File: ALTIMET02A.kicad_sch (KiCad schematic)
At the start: 11 parts

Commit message: Edit schema.
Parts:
- removed J? (x2): Conn_01x03_Male, symbol Connector:Conn_01x03_Male
- removed J? (x2): Conn_02x03_Odd_Even, symbol Connector_Generic:Conn_02x03_Odd_Even
- removed J?: Conn_02x06_Odd_Even, symbol Connector_Generic:Conn_02x06_Odd_Even
- added C?: 100nF, Capacitor_SMD:C_0805_2012Metric, symbol Device:C
- added J?: HEADER_2x05_PARALLEL, Mlab_Pin_Headers:Straight_2x05, symbol MLAB_HEADER:HEADER_2x05_PARALLEL
- added J?: HEADER_2x03_PARALLEL, Mlab_Pin_Headers:Straight_2x03, symbol MLAB_HEADER:HEADER_2x03_PARALLEL
- added J?: HEADER_2x03, Mlab_Pin_Headers:Straight_2x03, symbol MLAB_HEADER:HEADER_2x03
- added JP? (x2): SolderJumper_3_Bridged12, Jumper:SolderJumper-3_P1.3mm_Bridged12_RoundedPad1.0x1.5mm_NumberLabels, symbol Jumper:SolderJumper_3_Bridged12
- added JP?: SolderJumper_3_Bridged123, Jumper:SolderJumper-3_P1.3mm_Bridged12_RoundedPad1.0x1.5mm_NumberLabels, symbol Jumper:SolderJumper_3_Bridged123
- C?: value 100nF -> 10uF; footprint (none) -> Capacitor_SMD:C_0805_2012Metric
- H? (x4): footprint (none) -> Mlab_Mechanical:MountingHole_3mm
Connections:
- net CS/A: now also J?.5, JP?.2 (C), JP?.2 (C); no longer IC?.5 (CSB_2)
- net GND: now also C?.2, J?.1, J?.1, J?.10, J?.2, J?.2, J?.5, J?.6, J?.6, J?.9, JP?.1 (A), JP?.3 (B)
- net MISO: now also J?.1
- net MOSI/SDA: now also J?.4, J?.7, J?.8
- net PS: now also JP?.2 (C)
- net SCLK: now also J?.3, J?.3, J?.4
- net VDD: now also C?.1, J?.2, J?.3, J?.4, J?.5, J?.6, JP?.1 (A), JP?.3 (B)
- net CSB: no longer names the net of IC?.4 (CSB_1)
- net CSB: now also JP?.1 (A)
- new net: IC?.5 (CSB_2), JP?.3 (B)
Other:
- moved on the sheet: C?

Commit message: pcb layout
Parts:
- added R1, R2: 10k, Resistor_SMD:R_0805_2012Metric, symbol Device:R
- IC1: renamed from IC?; footprint MS561101BA03-50 -> KiCad:MS561101BA03-50
- gave numbers to parts that had none: 12
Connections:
- net MOSI/SDA: now also R2.2
- net SCLK: now also R1.2
- net VDD: now also R1.1, R2.1
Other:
- moved on the sheet: J2, J3

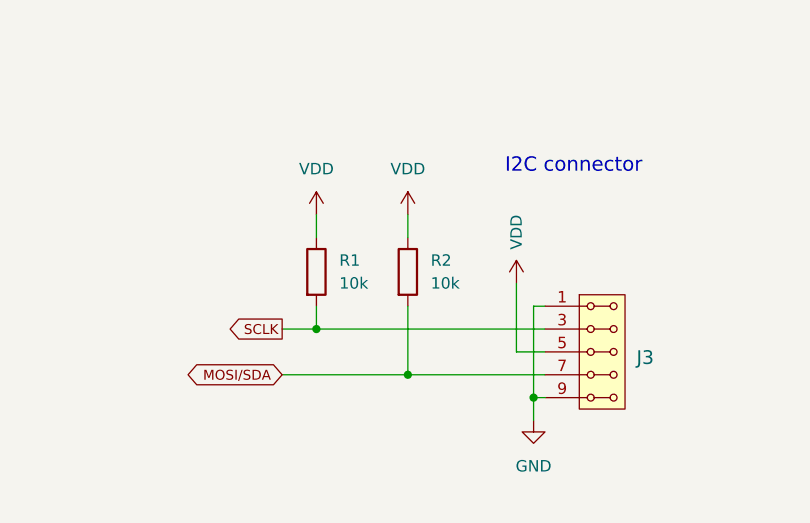
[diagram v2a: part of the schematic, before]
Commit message: DNF values added
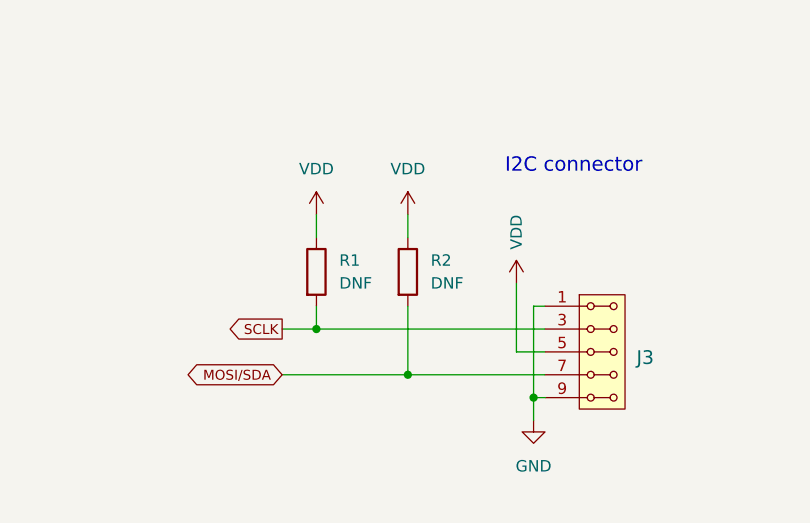
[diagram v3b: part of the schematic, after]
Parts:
- R1, R2: value 10k -> DNF
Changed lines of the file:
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@@
       (effects (font (size 1.27 1.27)) (justify left))
     )
-    (property "Value" "10k" (id 1) (at 237.49 121.9199 0)
+    (property "Value" "DNF" (id 1) (at 237.49 121.9199 0)
       (effects (font (size 1.27 1.27)) (justify left))
     )
@@
       (effects (font (size 1.27 1.27)) (justify left))
     )
-    (property "Value" "10k" (id 1) (at 227.33 121.9199 0)
+    (property "Value" "DNF" (id 1) (at 227.33 121.9199 0)
       (effects (font (size 1.27 1.27)) (justify left))
     )
@@
     )
     (path "/f13b7327-bb05-40fa-8b40-12fd0fcfee2c"
-      (reference "R1") (unit 1) (value "10k") (footprint "Resistor_SMD:R_0805_2012Metric")
+      (reference "R1") (unit 1) (value "DNF") (footprint "Resistor_SMD:R_0805_2012Metric")
     )
     (path "/46e25556-1506-4d58-a0a0-05cb5bee836e"
-      (reference "R2") (unit 1) (value "10k") (footprint "Resistor_SMD:R_0805_2012Metric")
-    )
-  )
+      (reference "R2") (unit 1) (value "DNF") (footprint "Resistor_SMD:R_0805_2012Metric")
+    )
+  )

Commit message: 3x1 layout
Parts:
- removed JP2: SolderJumper_3_Bridged123, Jumper:SolderJumper-3_P1.3mm_Bridged12_RoundedPad1.0x1.5mm_NumberLabels, symbol Jumper:SolderJumper_3_Bridged123
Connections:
- net CS/A: now also IC1.4 (CSB_1)
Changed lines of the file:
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@@
-    (stroke (width 0) (type default) (color 0 0 0 0))
-  )
-  (wire (pts (xy 124.46 83.82) (xy 128.27 83.82))
     (stroke (width 0) (type default) (color 0 0 0 0))
   )
@@
     (stroke (width 0) (type default) (color 0 0 0 0))
   )
-  (wire (pts (xy 163.83 83.82) (xy 163.83 92.075))
-    (stroke (width 0) (type default) (color 0 0 0 0))
-  )
   (wire (pts (xy 125.73 81.28) (xy 128.27 81.28))
     (stroke (width 0) (type default) (color 0 0 0 0))
@@
     (stroke (width 0) (type default) (color 0 0 0 0))
   )
-  (wire (pts (xy 124.46 92.075) (xy 139.065 92.075))
-    (stroke (width 0) (type default) (color 0 0 0 0))
-  )
   (wire (pts (xy 161.29 81.28) (xy 163.83 81.28))
     (stroke (width 0) (type default) (color 0 0 0 0))
@@
     (stroke (width 0) (type default) (color 0 0 0 0))
   )
-  (wire (pts (xy 124.46 83.82) (xy 124.46 92.075))
+  (wire (pts (xy 125.73 83.82) (xy 128.27 83.82))
     (stroke (width 0) (type default) (color 0 0 0 0))
   )
@@
     (stroke (width 0) (type default) (color 0 0 0 0))
   )
-  (wire (pts (xy 144.145 98.425) (xy 145.415 98.425))
-    (stroke (width 0) (type default) (color 0 0 0 0))
-  )
   (wire (pts (xy 250.19 124.46) (xy 248.92 124.46))
     (stroke (width 0) (type default) (color 0 0 0 0))
@@
     (stroke (width 0) (type default) (color 0 0 0 0))
   )
-  (wire (pts (xy 161.29 83.82) (xy 163.83 83.82))
-    (stroke (width 0) (type default) (color 0 0 0 0))
-  )
   (wire (pts (xy 166.37 131.445) (xy 166.37 137.16))
     (stroke (width 0) (type default) (color 0 0 0 0))
@@
     (stroke (width 0) (type default) (color 0 0 0 0))
   )
-  (wire (pts (xy 163.83 92.075) (xy 149.225 92.075))
-    (stroke (width 0) (type default) (color 0 0 0 0))
-  )
   (wire (pts (xy 253.365 84.455) (xy 253.365 81.915))
     (stroke (width 0) (type default) (color 0 0 0 0))
@@
   )
   (wire (pts (xy 261.62 34.29) (xy 261.62 36.83))
-    (stroke (width 0) (type default) (color 0 0 0 0))
-  )
-  (wire (pts (xy 144.145 95.885) (xy 144.145 98.425))
     (stroke (width 0) (type default) (color 0 0 0 0))
   )
@@
     )
   )
-  (global_label "CS{slash}A" (shape input) (at 145.415 98.425 0) (fields_autoplaced)
-    (effects (font (size 1.1 1.1)) (justify left))
-    (property "Intersheet References" "${INTERSHEET_REFS}" (id 0) (at 151.7479 98.3563 0)
-      (effects (font (size 1.1 1.1)) (justify left) hide)
+  (global_label "CS{slash}A" (shape input) (at 125.73 83.82 180) (fields_autoplaced)
+    (effects (font (size 1.1 1.1)) (justify right))
+    (property "Intersheet References" "${INTERSHEET_REFS}" (id 0) (at 119.3971 83.8887 0)
+      (effects (font (size 1.1 1.1)) (justify right) hide)
     )
   )
@@
     (pin "6")
   )
-  (symbol (lib_id "Jumper:SolderJumper_3_Bridged123") (at 144.145 92.075 0) (unit 1)
-    (in_bom yes) (on_board yes) (fields_autoplaced)
-    (property "Reference" "JP2" (id 0) (at 144.145 89.9945 0))
-    (property "Value" "SolderJumper_3_Bridged123" (id 1) (at 144.145 89.9946 0)
-      (effects (font (size 1.27 1.27)) hide)
-    )
-    (property "Footprint" "Jumper:SolderJumper-3_P1.3mm_Bridged12_RoundedPad1.0x1.5mm_NumberLabels" (id 2) (at 144.145 92.075 0)
-      (effects (font (size 1.27 1.27)) hide)
-    )
-    (property "Datasheet" "~" (id 3) (at 144.145 92.075 0)
-      (effects (font (size 1.27 1.27)) hide)
-    )
-    (pin "1")
-    (pin "2")
-    (pin "3")
-  )
   (symbol (lib_name "GND_2") (lib_id "power:GND") (at 86.995 81.28 0) (unit 1)
     (in_bom yes) (on_board yes) (fields_autoplaced)
@@
       (reference "JP1") (unit 1) (value "SolderJumper_3_Bridged12") (footprint "Jumper:SolderJumper-3_P1.3mm_Bridged12_RoundedPad1.0x1.5mm_NumberLabels")
     )
-    (path "/3d1603d1-143c-41d4-a06d-5e99796145c4"
-      (reference "JP2") (unit 1) (value "SolderJumper_3_Bridged123") (footprint "Jumper:SolderJumper-3_P1.3mm_Bridged12_RoundedPad1.0x1.5mm_NumberLabels")
-    )
     (path "/0a62873e-1f89-4b58-bf0c-fd0896fe225b"
